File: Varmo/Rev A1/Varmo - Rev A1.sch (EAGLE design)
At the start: 0 parts

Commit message: Add NTE0505MC todc-dc-converter library, add 82473C to murata inductor, update Varmo Rev A1 Sch
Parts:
- added C1, C2: 4.7uF, rcl:C-EUC0603
- added C3: 0.1uF, rcl:C-EUC0603
- added DC1: NTE0505MC, dc-dc-converter:NTE0505MC
- added OK1: HCPL2231, optocoupler:HCPL2231
- added OK2: HCPL2201, optocoupler:HCPL2201
- added U$1: 47uH, murata-inductance:82473C
- added X1: NC5FAV, con-neutrik_ag:NC5FAV
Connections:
- new net +5V: C2.1, C3.1, DC1.+VIN, X1.5
- new net +5V/1: C1.1, OK1A.VCC, U$1.2
- new net ESW3: X1.4
- new net ESW3_RX: OK1A.A, X1.2
- new net ESW3_RX_ISO: OK1A.OUT
- new net ESW3_TX: OK1B.A, X1.3
- new net ESW3_TX_ISO: OK1B.OUT
- new net GND: C2.2, C3.2, DC1.-VIN, OK1A.C, OK1B.C, X1.1
- new net GND1: C1.2, DC1.-VOUT, OK1A.GND
- new net GND2: X1.G
- new net N$1: DC1.+VOUT, U$1.1

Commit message: Update Varmo schematic Rev A1
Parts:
- removed OK2: HCPL2201, optocoupler:HCPL2201
- removed X1: NC5FAV, con-neutrik_ag:NC5FAV
- added C4, C5, C6: 0.1uF, rcl:C-EUC0603
- added OK3: HCPL2201300E, optocoupler:HCPL2201300E
- added U1: ATMEGA168, atmel:ATMEGA168
- added X2: NC5MAV-SW, con-neutrik_ag:NC5MAV-SW
- added Y1: 10MHz, resonator:RESONATOR1:1
- OK1: value HCPL2231 -> HCPL2231300E; device optocoupler:HCPL2231 -> optocoupler:HCPL2231300E
- renumbered U$1 to L1
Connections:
- removed net ESW3: X1.4
- removed net ESW3_RX: OK1A.A, X1.2
- new net ESW3_ISO: OK1B.A, OK1B.OUT, X2-1.4
- new net N$2: U1.PB6(XTAL1/TOSC1), Y1.1
- new net N$3: U1.PB7(XTAL2/TOSC2), Y1.3
- net +5V: now also OK1A.VCC, X2-1.5; no longer X1.5
- net +5V/1: now also C4.1, C5.1, C6.1, OK3.VCC, U1.AVCC, U1.VCC@1, U1.VCC@2; no longer OK1A.VCC
- net ESW3_RX_ISO: now also OK1A.A, X2-1.2
- net ESW3_TX: now also OK3.A, X2-1.3; no longer OK1B.A, X1.3
- net ESW3_TX_ISO: now also OK3.OUT; no longer OK1B.OUT
- net GND: now also OK1A.GND, OK3.C, X2-1.1; no longer OK1A.C, OK1B.C, X1.1
- net GND1: now also C4.2, C5.2, C6.2, OK1A.C, OK1B.C, OK3.GND, U1.AGND, U1.GND@1, U1.GND@2, Y1.2; no longer OK1A.GND
- net GND2: now also X2-1.G; no longer X1.G

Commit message: Update Varmo schematic, add library for screw connector , add library for encoder, add library for potentiometre
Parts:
- added C10, C7, C8, C9: 0.1uF, rcl:C-EUC0603
- added JP1: F-2X3, con-headers-jp:F-2X3
- added JP2: (no value), pinhead:PINHD-1X16
- added R1, R2, R3, R8: 10K, rcl:R-EU_R0603
- added R10, R7, R9: 4.7k, rcl:R-EU_R0603
- added R4, R5: 2.2K, rcl:R-EU_R0603
- added R6: 3313J-1-203E, pot:3313J-1-203E
- added U$1: EC11E18244AU, encoder:EC11E18244AU
- added X1: NC5MAH, con-neutrik_ag:NC5MAH
- added X3, X4: SMKDSP_1,5/2, con-phoenix-smkdsp:SMKDSP_1,5/2
- U1: value ATMEGA168 -> ATMEGA328
- X2: value NC5MAV-SW -> SMKDSP_1,5/3; device con-neutrik_ag:NC5MAV-SW -> con-phoenix-smkdsp:SMKDSP_1,5/3
- Y1: value 10MHz -> 8MHz; device resonator:RESONATOR1:1 -> resonator:RESONATORSMD
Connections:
- new net DIRECTION_1: R8.1, X2-1.KL
- new net DIRECTION_2: R7.1, X2-2.KL
- new net ENCODER_A: U1.PC0(ADC0)
- new net ENCODER_B: U1.PC1(ADC1)
- new net ENCODER_C: U1.PC2(ADC2)
- new net MISO: JP1.1, U1.PB4(MISO)
- new net MOSI: JP1.3, U1.PB3(MOSI/OC2)
- new net N$4: C9.1, JP1.6
- new net N$5: C10.1, U1.AREF
- new net PUSH_BUTTON_1: R9.1, X3-1.KL
- new net PUSH_BUTTON_2: R10.1, X4-1.KL
- new net RESET: JP1.4, R1.1, U1.PC6(/RESET)
- new net SA0: JP2.7, R2.2
- new net SA1: JP2.8, R3.2
- new net SCK: JP1.5, U1.PB5(SCK)
- new net SCL: JP2.14, R5.1, U1.PC5(ADC5/SCL)
- new net SDA: JP2.13, R4.1, U1.PC4(ADC4/SDA)
- new net VEE: JP2.15, R6.A
- new net VO: JP2.3, R6.S
- net +5V: now also C8.1, X1.5; no longer X2-1.5
- net +5V/1: now also C7.1, JP1.2, JP2.2, R1.2, R10.2, R4.2, R5.2, R6.E, R7.2, R8.2, R9.2
- net ESW3_ISO: now also U1.PD2(INT0), X1.4; no longer X2-1.4
- net ESW3_RX_ISO: now also U1.PD1(TXD), X1.2; no longer X2-1.2
- net ESW3_TX: now also X1.3; no longer X2-1.3
- net ESW3_TX_ISO: now also U1.PD0(RXD)
- net GND: now also C8.2, X1.1; no longer X2-1.1
- net GND1: now also C10.2, C7.2, C9.2, JP2.1, JP2.12, JP2.16, R2.1, R3.1, X2-3.KL, X3-2.KL, X4-2.KL
- net GND2: now also X1.G; no longer X2-1.G
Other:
- note added: "DC-DC convertor"
- note added: "LCD SCREEN CONNECTOR"
- note added: "LCD SCREEN CONTRAST"
- note added: "SIGNAL ISOLATION"
- moved on the sheet: C4, C5, C6, U1, Y1

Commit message: Update murata inductance.lbr (footprint serie 8400), Update of the Varmo - Rev A1 schematic, Add schmitt trigger x2 and x3 to ti.lbr
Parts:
- added C11, C12, C13, C14, C15, C16: 0.1uF, rcl:C-EUC0603
- added LED1, LED2, LED3, LED4: Blue, led:LEDCHIP-LED0603
- added LED5: GRN, led:LED10MM
- added LED6: RED, led:LED10MM
- added R11, R13, R14, R15, R16, R17, R21, R22, R23, R24: 4.7k, rcl:R-EU_R0603
- added R12: 4.7K, rcl:R-EU_R0603
- added R18, R19, R20, R25, R26: 0, rcl:R-EU_R0603
- added U2, U3: SN74LVC2G17DBVR, ti:SN74LVC2G17DBVR
- added U4, U5: 90814-0210, Molex_By_element14_Batch_1:90814-0210
- R8: value 10K -> 4.7K
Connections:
- removed net ENCODER_C: U1.PC2(ADC2)
- new net 5V: R24.2, U4.8, X1.5
- new net BUTTON_1: R19.2, U1.PC0(ADC0)
- new net CONSTRASTE: U1.PB1(OC1A)
- new net CONTRASTE: R26.2
- new net ENCODER_E: R13.1, U$1.P$2, U1.PD4(XCK/T0)
- new net ESW3: OK1B.OUT, U5.6
- new net ESW3_CMD: R20.1, U1.PD5(T1)
- new net ESW3_RX: OK1A.OUT, U5.2
- new net N$10: C13.1, R16.2, U2.1A
- new net N$11: C14.1, R17.2, U2.2A
- new net N$12: C12.1, R15.2, U3.2A
- new net N$13: C11.1, R14.2, U3.1A
- new net N$14: R25.2, R6.S
- new net N$18: LED1.A, R21.1
- new net N$19: LED2.A, R22.1
- new net N$20: LED3.A, R23.1
- new net N$21: LED4.A, R24.1
- new net N$6: R10.1, R15.1, X4-1.KL
- new net N$7: R14.1, R9.1, X3-1.KL
- new net N$8: R16.1, R7.1, X2-1.KL
- new net N$9: R17.1, R8.1, X2-2.KL
- new net RX: R21.2, U4.2, X1.2
- new net TOR: R23.2, U4.6, X1.4
- new net TX: R22.2, U4.4, X1.3
- net +5V: now also U5.8; no longer X1.5
- net +5V/1: now also C15.1, C16.1, R11.2, R12.2, R13.2, U2.VCC, U3.VCC
- net DIRECTION_1: now also U1.PC2(ADC2), U2.1Y; no longer R8.1, X2-1.KL
- net DIRECTION_2: now also U1.PC3(ADC3), U2.2Y; no longer R7.1, X2-2.KL
- net ENCODER_A: now also R11.1, U$1.P$4, U1.PD2(INT0); no longer U1.PC0(ADC0)
- net ENCODER_B: now also R12.1, U$1.P$5, U1.PD3(INT1); no longer U1.PC1(ADC1)
- net ESW3_ISO: now also R18.2, R20.2; no longer OK1B.OUT, U1.PD2(INT0), X1.4
- net ESW3_RX_ISO: no longer OK1A.OUT, X1.2
- net ESW3_TX: now also U5.4; no longer X1.3
- net GND: now also LED1.C, LED2.C, LED3.C, LED4.C, U4.1, U4.10, U4.3, U4.5, U4.7, U4.9, U5.1, U5.10, U5.3, U5.5, U5.7, U5.9
- net GND1: now also C11.2, C12.2, C13.2, C14.2, C15.2, C16.2, U$1.P$1, U$1.P$3, U2.GND, U3.GND
- net PUSH_BUTTON_1: now also R18.1, R19.1, U3.1Y; no longer R9.1, X3-1.KL
- net PUSH_BUTTON_2: now also U1.PC1(ADC1), U3.2Y; no longer R10.1, X4-1.KL
- net VO: now also R25.1, R26.1; no longer R6.S
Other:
- moved on the sheet: C1, C10, C2, C3, C4, C5, C6, C7, C8, C9, DC1, JP1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

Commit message: Update of Varmo - Rev A1 schematic
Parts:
- added R27, R28: 1.5k, rcl:R-EU_R0603
- R21, R22, R23, R24: value 4.7k -> 1.5k
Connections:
- new net LED_1: R28.2, U1.ADC6
- new net LED_2: R27.2, U1.ADC7
- new net N$15: LED5.A, R27.1
- new net N$16: LED6.A, R28.1
- net GND: now also LED5.C, LED6.C
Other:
- moved on the sheet: LED5, LED6, R18, R19, R20
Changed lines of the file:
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@@
 <part name="LED3" library="led" deviceset="LED" device="CHIP-LED0603" value="Blue"/>
 <part name="LED4" library="led" deviceset="LED" device="CHIP-LED0603" value="Blue"/>
-<part name="R21" library="rcl" deviceset="R-EU_" device="R0603" value="4.7k"/>
-<part name="R22" library="rcl" deviceset="R-EU_" device="R0603" value="4.7k"/>
-<part name="R23" library="rcl" deviceset="R-EU_" device="R0603" value="4.7k"/>
-<part name="R24" library="rcl" deviceset="R-EU_" device="R0603" value="4.7k"/>
+<part name="R21" library="rcl" deviceset="R-EU_" device="R0603" value="1.5k"/>
+<part name="R22" library="rcl" deviceset="R-EU_" device="R0603" value="1.5k"/>
+<part name="R23" library="rcl" deviceset="R-EU_" device="R0603" value="1.5k"/>
+<part name="R24" library="rcl" deviceset="R-EU_" device="R0603" value="1.5k"/>
 <part name="SUPPLY51" library="supply2" deviceset="GND" device=""/>
 <part name="U$1" library="encoder" deviceset="EC11E?" device="18244AU"/>
@@
 <part name="LED5" library="led" deviceset="LED" device="10MM" value="GRN"/>
 <part name="LED6" library="led" deviceset="LED" device="10MM" value="RED"/>
+<part name="R27" library="rcl" deviceset="R-EU_" device="R0603" value="1.5k"/>
+<part name="R28" library="rcl" deviceset="R-EU_" device="R0603" value="1.5k"/>
+<part name="SUPPLY52" library="supply2" deviceset="GND" device=""/>
+<part name="SUPPLY53" library="supply2" deviceset="GND" device=""/>
 </parts>
 <sheets>
@@
 <instance part="SUPPLY47" gate="G$1" x="289.56" y="93.98"/>
 <instance part="C16" gate="G$1" x="289.56" y="104.14"/>
-<instance part="R18" gate="G$1" x="193.04" y="27.94" rot="R180"/>
-<instance part="R19" gate="G$1" x="193.04" y="20.32" rot="R180"/>
-<instance part="R20" gate="G$1" x="193.04" y="35.56" rot="R180"/>
+<instance part="R18" gate="G$1" x="215.9" y="38.1" rot="R180"/>
+<instance part="R19" gate="G$1" x="215.9" y="30.48" rot="R180"/>
+<instance part="R20" gate="G$1" x="215.9" y="45.72" rot="R180"/>
 <instance part="U4" gate="A" x="83.82" y="231.14" rot="MR0"/>
 <instance part="U5" gate="A" x="40.64" y="170.18"/>
@@
 <instance part="R25" gate="G$1" x="340.36" y="228.6" rot="R180"/>
 <instance part="R26" gate="G$1" x="340.36" y="236.22" rot="R180"/>
-<instance part="LED5" gate="G$1" x="50.8" y="127"/>
-<instance part="LED6" gate="G$1" x="66.04" y="127"/>
+<instance part="LED5" gate="G$1" x="149.86" y="38.1"/>
+<instance part="LED6" gate="G$1" x="165.1" y="38.1"/>
+<instance part="R27" gate="G$1" x="149.86" y="48.26" rot="R90"/>
+<instance part="R28" gate="G$1" x="165.1" y="48.26" rot="R90"/>
+<instance part="SUPPLY52" gate="GND" x="149.86" y="27.94"/>
+<instance part="SUPPLY53" gate="GND" x="165.1" y="27.94"/>
 </instances>
 <busses>
@@
 <junction x="45.72" y="195.58"/>
 </segment>
+<segment>
+<pinref part="LED5" gate="G$1" pin="C"/>
+<pinref part="SUPPLY52" gate="GND" pin="GND"/>
+<wire x1="149.86" y1="33.02" x2="149.86" y2="30.48" width="0.1524" layer="91"/>
+</segment>
+<segment>
+<pinref part="SUPPLY53" gate="GND" pin="GND"/>
+<pinref part="LED6" gate="G$1" pin="C"/>
+<wire x1="165.1" y1="30.48" x2="165.1" y2="33.02" width="0.1524" layer="91"/>
+</segment>
 </net>
 <net name="GND2" class="0">
@@
 <segment>
 <pinref part="R20" gate="G$1" pin="2"/>
-<label x="182.88" y="27.94" size="1.27" layer="95" rot="R180" xref="yes"/>
-<wire x1="187.96" y1="27.94" x2="185.42" y2="27.94" width="0.1524" layer="91"/>
-<wire x1="185.42" y1="27.94" x2="182.88" y2="27.94" width="0.1524" layer="91"/>
-<wire x1="187.96" y1="35.56" x2="185.42" y2="35.56" width="0.1524" layer="91"/>
-<wire x1="185.42" y1="35.56" x2="185.42" y2="27.94" width="0.1524" layer="91"/>
-<junction x="185.42" y="27.94"/>
+<label x="205.74" y="38.1" size="1.27" layer="95" rot="R180" xref="yes"/>
+<wire x1="210.82" y1="38.1" x2="208.28" y2="38.1" width="0.1524" layer="91"/>
+<wire x1="208.28" y1="38.1" x2="205.74" y2="38.1" width="0.1524" layer="91"/>
+<wire x1="210.82" y1="45.72" x2="208.28" y2="45.72" width="0.1524" layer="91"/>
+<wire x1="208.28" y1="45.72" x2="208.28" y2="38.1" width="0.1524" layer="91"/>
+<junction x="208.28" y="38.1"/>
 <pinref part="R18" gate="G$1" pin="2"/>
 </segment>
@@
 <segment>
 <pinref part="R19" gate="G$1" pin="1"/>
-<junction x="203.2" y="27.94"/>
-<label x="210.82" y="27.94" size="1.27" layer="95" xref="yes"/>
-<wire x1="198.12" y1="20.32" x2="203.2" y2="20.32" width="0.1524" layer="91"/>
-<wire x1="203.2" y1="20.32" x2="203.2" y2="27.94" width="0.1524" layer="91"/>
-<wire x1="203.2" y1="27.94" x2="210.82" y2="27.94" width="0.1524" layer="91"/>
-<wire x1="198.12" y1="27.94" x2="203.2" y2="27.94" width="0.1524" layer="91"/>
+<junction x="226.06" y="38.1"/>
+<label x="233.68" y="38.1" size="1.27" layer="95" xref="yes"/>
+<wire x1="220.98" y1="30.48" x2="226.06" y2="30.48" width="0.1524" layer="91"/>
+<wire x1="226.06" y1="30.48" x2="226.06" y2="38.1" width="0.1524" layer="91"/>
+<wire x1="226.06" y1="38.1" x2="233.68" y2="38.1" width="0.1524" layer="91"/>
+<wire x1="220.98" y1="38.1" x2="226.06" y2="38.1" width="0.1524" layer="91"/>
 <pinref part="R18" gate="G$1" pin="1"/>
 </segment>
@@
 <segment>
 <pinref part="R19" gate="G$1" pin="2"/>
-<label x="182.88" y="20.32" size="1.27" layer="95" rot="R180" xref="yes"/>
-<wire x1="187.96" y1="20.32" x2="182.88" y2="20.32" width="0.1524" layer="91"/>
+<label x="205.74" y="30.48" size="1.27" layer="95" rot="R180" xref="yes"/>
+<wire x1="210.82" y1="30.48" x2="205.74" y2="30.48" width="0.1524" layer="91"/>
 </segment>
 <segment>
@@
 <segment>
 <pinref part="R20" gate="G$1" pin="1"/>
-<wire x1="198.12" y1="35.56" x2="210.82" y2="35.56" width="0.1524" layer="91"/>
-<label x="210.82" y="35.56" size="1.27" layer="95" xref="yes"/>
+<wire x1="220.98" y1="45.72" x2="233.68" y2="45.72" width="0.1524" layer="91"/>
+<label x="233.68" y="45.72" size="1.27" layer="95" xref="yes"/>
 </segment>
 <segment>
@@
 </segment>
 </net>
+<net name="N$15" class="0">
+<segment>
+<pinref part="LED5" gate="G$1" pin="A"/>
+<pinref part="R27" gate="G$1" pin="1"/>
+<wire x1="149.86" y1="43.18" x2="149.86" y2="40.64" width="0.1524" layer="91"/>
+</segment>
+</net>
+<net name="N$16" class="0">
+<segment>
+<pinref part="LED6" gate="G$1" pin="A"/>
+<pinref part="R28" gate="G$1" pin="1"/>
+<wire x1="165.1" y1="43.18" x2="165.1" y2="40.64" width="0.1524" layer="91"/>
+</segment>
+</net>
+<net name="LED_1" class="0">
+<segment>
+<pinref part="U1" gate="G$1" pin="ADC6"/>
+<pinref part="R28" gate="G$1" pin="2"/>
+<wire x1="124.46" y1="58.42" x2="165.1" y2="58.42" width="0.1524" layer="91"/>
+<wire x1="165.1" y1="58.42" x2="165.1" y2="53.34" width="0.1524" layer="91"/>
+<label x="124.46" y="58.42" size="1.778" layer="95"/>
+</segment>
+</net>
+<net name="LED_2" class="0">
+<segment>
+<pinref part="R27" gate="G$1" pin="2"/>
+<pinref part="U1" gate="G$1" pin="ADC7"/>
+<wire x1="124.46" y1="55.88" x2="149.86" y2="55.88" width="0.1524" layer="91"/>
+<wire x1="149.86" y1="55.88" x2="149.86" y2="53.34" width="0.1524" layer="91"/>
+<label x="124.46" y="55.88" size="1.778" layer="95"/>
+</segment>
+</net>

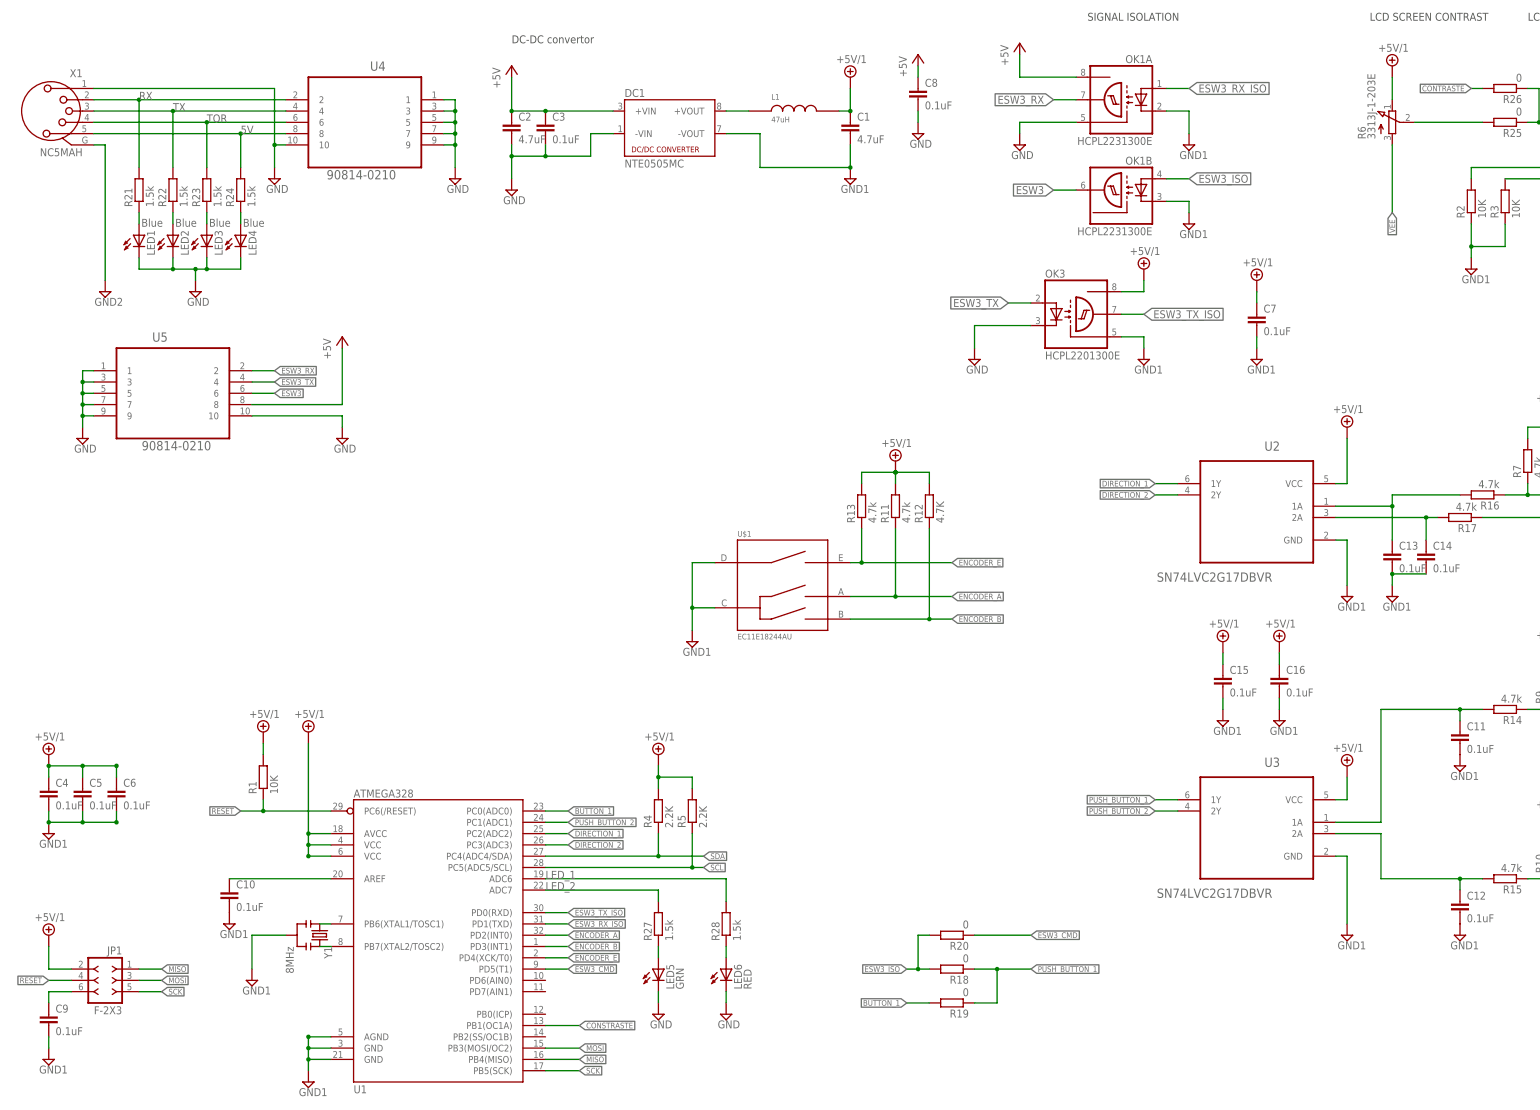
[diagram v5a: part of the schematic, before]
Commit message: Update International_Rectfier_By_element14_Batch_1.lbr, Update Varmo Rev A1 schematic
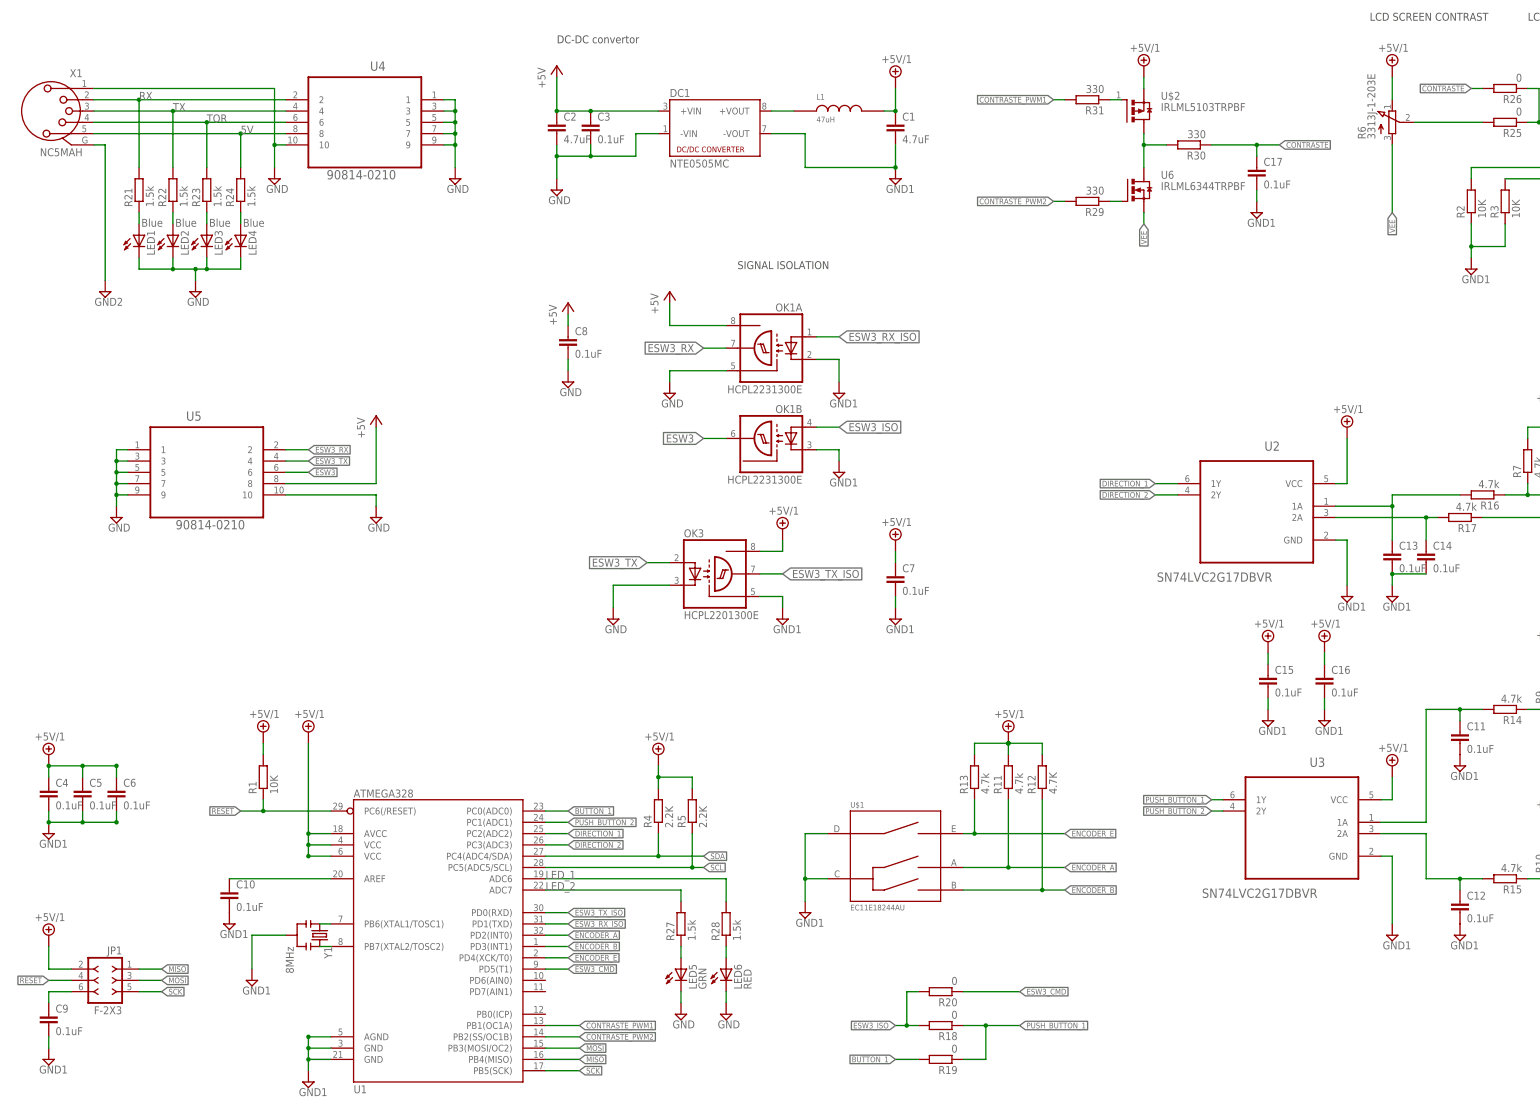
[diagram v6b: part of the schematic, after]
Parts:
- added C17: 0.1uF, rcl:C-EUC0603
- added R29, R30, R31: 330, rcl:R-EU_R0603
- added U$2: IRLML5103TRPBF, International_Rectifier_By_element14_Batch_1:IRLML5103TRPBF
- added U6: IRLML6344TRPBF, International_Rectifier_By_element14_Batch_1:IRLML6344TRPBF
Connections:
- removed net CONSTRASTE: U1.PB1(OC1A)
- new net CONTRASTE_PWM1: R31.2, U1.PB1(OC1A)
- new net CONTRASTE_PWM2: R29.2, U1.PB2(SS/OC1B)
- new net N$17: R29.1, U6.G
- new net N$22: R30.2, U$2.D, U6.D
- new net N$24: R31.1, U$2.G
- net +5V/1: now also U$2.S
- net CONTRASTE: now also C17.1, R30.1
- net GND1: now also C17.2
- net VEE: now also U6.S
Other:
- moved on the sheet: C1, C15, C16, C2, C3, C7, C8, DC1, L1, LED5, OK1A, OK1B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
